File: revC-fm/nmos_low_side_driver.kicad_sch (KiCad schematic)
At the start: 6 parts, among them Q48 MMBT2907AM3T5G, Q49 MMDT3946

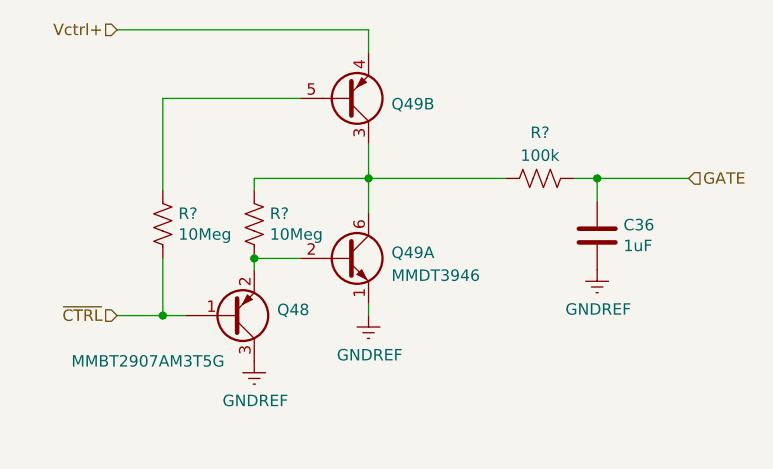
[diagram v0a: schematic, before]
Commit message: updated analog , solar comp, layout
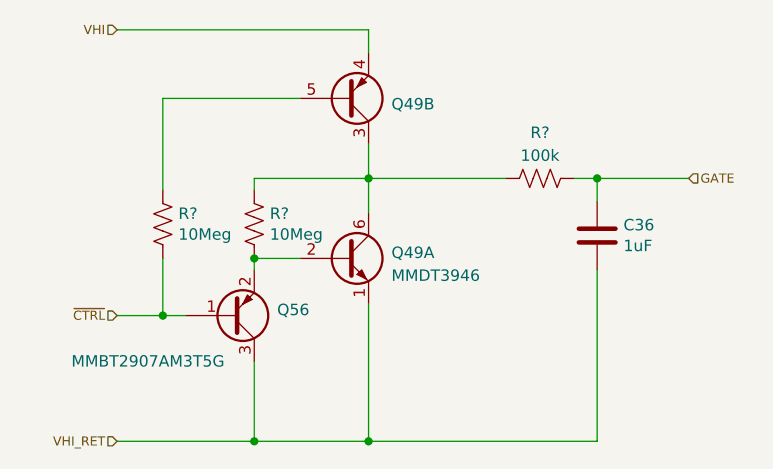
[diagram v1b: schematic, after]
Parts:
- renumbered Q48 to Q56
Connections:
- net GNDREF renamed VHI_RET
- net Vctrl+ renamed VHI

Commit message: routing
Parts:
- renumbered Q56 to Q58
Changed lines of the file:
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@@
         )
         (path "/d1441985-7b63-4bf8-a06d-c70da2e3b78b/00000000-0000-0000-0000-00005cec5dde/108189db-ac43-429a-bea6-7a20153b7e07/9a2f7458-daa0-4897-b1a7-e66c6dd2d928"
-          (reference "R219") (unit 1)
+          (reference "R213") (unit 1)
         )
       )
@@
         )
         (path "/d1441985-7b63-4bf8-a06d-c70da2e3b78b/00000000-0000-0000-0000-00005cec5dde/108189db-ac43-429a-bea6-7a20153b7e07/9a2f7458-daa0-4897-b1a7-e66c6dd2d928"
-          (reference "R220") (unit 1)
+          (reference "R214") (unit 1)
         )
       )
@@
   (symbol (lib_id "Device:Q_PNP_BEC") (at 120.65 105.41 0) (mirror x) (unit 1)
     (in_bom yes) (on_board yes) (dnp no)
-    (property "Reference" "Q56" (at 125.73 104.775 0)
+    (property "Reference" "Q58" (at 125.73 104.775 0)
       (effects (font (size 1.27 1.27)) (justify left))
     )
@@
       (project "mainboard"
         (path "/d1441985-7b63-4bf8-a06d-c70da2e3b78b/00000000-0000-0000-0000-00005cec5dde/108189db-ac43-429a-bea6-7a20153b7e07/9a2f7458-daa0-4897-b1a7-e66c6dd2d928"
-          (reference "Q56") (unit 1)
+          (reference "Q58") (unit 1)
         )
       )
@@
         )
         (path "/d1441985-7b63-4bf8-a06d-c70da2e3b78b/00000000-0000-0000-0000-00005cec5dde/108189db-ac43-429a-bea6-7a20153b7e07/9a2f7458-daa0-4897-b1a7-e66c6dd2d928"
-          (reference "R221") (unit 1)
+          (reference "R212") (unit 1)
         )
       )
@@
           (reference "C36") (unit 1)
         )
-        (path "/d1441985-7b63-4bf8-a06d-c70da2e3b78b/00000000-0000-0000-0000-00005cec5dde/b26c7749-01c8-494d-9e2e-e06c56569424"
-          (reference "C87") (unit 1)
-        )
         (path "/d1441985-7b63-4bf8-a06d-c70da2e3b78b/00000000-0000-0000-0000-00005cec5dde/108189db-ac43-429a-bea6-7a20153b7e07"
           (reference "C?") (unit 1)
@@
         )
         (path "/d1441985-7b63-4bf8-a06d-c70da2e3b78b/00000000-0000-0000-0000-00005cec5dde/108189db-ac43-429a-bea6-7a20153b7e07/9a2f7458-daa0-4897-b1a7-e66c6dd2d928"
-          (reference "C110") (unit 1)
-        )
-      )
+          (reference "C124") (unit 1)
+        )
+      )

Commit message: changed RF connector to TH
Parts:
- Q57: renamed from Q58; footprint Package_TO_SOT_SMD:SOT-723 -> SierraLobo:SOT-723
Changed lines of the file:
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@@
+      (effects (font (size 1.27 1.27)) hide)
+    )
+    (property "Mfr. Part No" "" (at 113.03 95.25 0)
       (effects (font (size 1.27 1.27)) hide)
     )
@@
         )
         (path "/d1441985-7b63-4bf8-a06d-c70da2e3b78b/00000000-0000-0000-0000-00005cec5dde/108189db-ac43-429a-bea6-7a20153b7e07/9a2f7458-daa0-4897-b1a7-e66c6dd2d928"
-          (reference "R213") (unit 1)
+          (reference "R209") (unit 1)
         )
       )
@@
     )
     (property "Datasheet" "http://www.diodes.com/_files/datasheets/ds30123.pdf" (at 133.35 99.06 0)
+      (effects (font (size 1.27 1.27)) hide)
+    )
+    (property "Mfr. Part No" "" (at 133.35 99.06 0)
       (effects (font (size 1.27 1.27)) hide)
     )
@@
         )
         (path "/d1441985-7b63-4bf8-a06d-c70da2e3b78b/00000000-0000-0000-0000-00005cec5dde/108189db-ac43-429a-bea6-7a20153b7e07/9a2f7458-daa0-4897-b1a7-e66c6dd2d928"
+          (reference "Q56") (unit 1)
+        )
+      )
+    )
+  )
+  (symbol (lib_id "Device:R_US") (at 123.19 95.25 0) (unit 1)
+    (in_bom yes) (on_board yes) (dnp no)
+    (property "Reference" "R?" (at 124.9172 94.0816 0)
+      (effects (font (size 1.27 1.27)) (justify left))
+    )
+    (property "Value" "10Meg" (at 124.9172 96.393 0)
+      (effects (font (size 1.27 1.27)) (justify left))
+    )
+    (property "Footprint" "Resistor_SMD:R_0603_1608Metric" (at 124.206 95.504 90)
+      (effects (font (size 1.27 1.27)) hide)
+    )
+    (property "Datasheet" "~" (at 123.19 95.25 0)
+      (effects (font (size 1.27 1.27)) hide)
+    )
+    (property "Mfr. Part No" "" (at 123.19 95.25 0)
+      (effects (font (size 1.27 1.27)) hide)
+    )
+    (pin "1")
+    (pin "2")
+    (instances
+      (project "mainboard"
+        (path "/d1441985-7b63-4bf8-a06d-c70da2e3b78b/00000000-0000-0000-0000-00005cec5dde/108189db-ac43-429a-bea6-7a20153b7e07"
+          (reference "R?") (unit 1)
+        )
+        (path "/d1441985-7b63-4bf8-a06d-c70da2e3b78b/00000000-0000-0000-0000-00005cec5dde/108189db-ac43-429a-bea6-7a20153b7e07/ea6bccc4-7d11-4c72-aac6-c14ca6d386f6"
+          (reference "R215") (unit 1)
+        )
+        (path "/d1441985-7b63-4bf8-a06d-c70da2e3b78b/00000000-0000-0000-0000-00005cec5dde/108189db-ac43-429a-bea6-7a20153b7e07/b16406a3-1a56-4ff9-817d-a6e31635f1dc"
+          (reference "R171") (unit 1)
+        )
+        (path "/d1441985-7b63-4bf8-a06d-c70da2e3b78b/00000000-0000-0000-0000-00005cec5dde/108189db-ac43-429a-bea6-7a20153b7e07/98075574-42bb-442c-ab5b-88185f36e4d7"
+          (reference "R177") (unit 1)
+        )
+        (path "/d1441985-7b63-4bf8-a06d-c70da2e3b78b/00000000-0000-0000-0000-00005cec5dde/108189db-ac43-429a-bea6-7a20153b7e07/58a3edb7-dfb1-4add-9075-2361d73480a6"
+          (reference "R204") (unit 1)
+        )
+        (path "/d1441985-7b63-4bf8-a06d-c70da2e3b78b/00000000-0000-0000-0000-00005cec5dde/108189db-ac43-429a-bea6-7a20153b7e07/68cb1cfa-66f3-4079-aaa8-5081a46702c5"
+          (reference "R183") (unit 1)
+        )
+        (path "/d1441985-7b63-4bf8-a06d-c70da2e3b78b/00000000-0000-0000-0000-00005cec5dde/108189db-ac43-429a-bea6-7a20153b7e07/9a2f7458-daa0-4897-b1a7-e66c6dd2d928"
+          (reference "R210") (unit 1)
+        )
+      )
+    )
+  )
+  (symbol (lib_id "Device:Q_PNP_BEC") (at 120.65 105.41 0) (mirror x) (unit 1)
+    (in_bom yes) (on_board yes) (dnp no)
+    (property "Reference" "Q57" (at 125.73 104.775 0)
+      (effects (font (size 1.27 1.27)) (justify left))
+    )
+    (property "Value" "MMBT2907AM3T5G" (at 102.87 110.49 0)
+      (effects (font (size 1.27 1.27)) (justify left))
+    )
+    (property "Footprint" "SierraLobo:SOT-723" (at 125.73 107.95 0)
+      (effects (font (size 1.27 1.27)) hide)
+    )
+    (property "Datasheet" "MMBT2907AM3T5G" (at 120.65 105.41 0)
+      (effects (font (size 1.27 1.27)) hide)
+    )
+    (property "Mfr. Part No" "" (at 120.65 105.41 0)
+      (effects (font (size 1.27 1.27)) hide)
+    )
+    (pin "1")
+    (pin "2")
+    (pin "3")
+    (instances
+      (project "mainboard"
+        (path "/d1441985-7b63-4bf8-a06d-c70da2e3b78b/00000000-0000-0000-0000-00005cec5dde/108189db-ac43-429a-bea6-7a20153b7e07/9a2f7458-daa0-4897-b1a7-e66c6dd2d928"
           (reference "Q57") (unit 1)
-        )
-      )
-    )
-  )
-  (symbol (lib_id "Device:R_US") (at 123.19 95.25 0) (unit 1)
-    (in_bom yes) (on_board yes) (dnp no)
-    (property "Reference" "R?" (at 124.9172 94.0816 0)
-      (effects (font (size 1.27 1.27)) (justify left))
-    )
-    (property "Value" "10Meg" (at 124.9172 96.393 0)
-      (effects (font (size 1.27 1.27)) (justify left))
-    )
-    (property "Footprint" "Resistor_SMD:R_0603_1608Metric" (at 124.206 95.504 90)
-      (effects (font (size 1.27 1.27)) hide)
-    )
-    (property "Datasheet" "~" (at 123.19 95.25 0)
-      (effects (font (size 1.27 1.27)) hide)
-    )
-    (pin "1")
-    (pin "2")
-    (instances
-      (project "mainboard"
-        (path "/d1441985-7b63-4bf8-a06d-c70da2e3b78b/00000000-0000-0000-0000-00005cec5dde/108189db-ac43-429a-bea6-7a20153b7e07"
-          (reference "R?") (unit 1)
-        )
-        (path "/d1441985-7b63-4bf8-a06d-c70da2e3b78b/00000000-0000-0000-0000-00005cec5dde/108189db-ac43-429a-bea6-7a20153b7e07/ea6bccc4-7d11-4c72-aac6-c14ca6d386f6"
-          (reference "R215") (unit 1)
-        )
-        (path "/d1441985-7b63-4bf8-a06d-c70da2e3b78b/00000000-0000-0000-0000-00005cec5dde/108189db-ac43-429a-bea6-7a20153b7e07/b16406a3-1a56-4ff9-817d-a6e31635f1dc"
-          (reference "R171") (unit 1)
-        )
-        (path "/d1441985-7b63-4bf8-a06d-c70da2e3b78b/00000000-0000-0000-0000-00005cec5dde/108189db-ac43-429a-bea6-7a20153b7e07/98075574-42bb-442c-ab5b-88185f36e4d7"
-          (reference "R177") (unit 1)
-        )
-        (path "/d1441985-7b63-4bf8-a06d-c70da2e3b78b/00000000-0000-0000-0000-00005cec5dde/108189db-ac43-429a-bea6-7a20153b7e07/58a3edb7-dfb1-4add-9075-2361d73480a6"
-          (reference "R204") (unit 1)
-        )
-        (path "/d1441985-7b63-4bf8-a06d-c70da2e3b78b/00000000-0000-0000-0000-00005cec5dde/108189db-ac43-429a-bea6-7a20153b7e07/68cb1cfa-66f3-4079-aaa8-5081a46702c5"
-          (reference "R183") (unit 1)
-        )
-        (path "/d1441985-7b63-4bf8-a06d-c70da2e3b78b/00000000-0000-0000-0000-00005cec5dde/108189db-ac43-429a-bea6-7a20153b7e07/9a2f7458-daa0-4897-b1a7-e66c6dd2d928"
-          (reference "R214") (unit 1)
-        )
-      )
-    )
-  )
-  (symbol (lib_id "Device:Q_PNP_BEC") (at 120.65 105.41 0) (mirror x) (unit 1)
-    (in_bom yes) (on_board yes) (dnp no)
-    (property "Reference" "Q58" (at 125.73 104.775 0)
-      (effects (font (size 1.27 1.27)) (justify left))
-    )
-    (property "Value" "MMBT2907AM3T5G" (at 102.87 110.49 0)
-      (effects (font (size 1.27 1.27)) (justify left))
-    )
-    (property "Footprint" "Package_TO_SOT_SMD:SOT-723" (at 125.73 107.95 0)
-      (effects (font (size 1.27 1.27)) hide)
-    )
-    (property "Datasheet" "MMBT2907AM3T5G" (at 120.65 105.41 0)
-      (effects (font (size 1.27 1.27)) hide)
-    )
-    (pin "1")
-    (pin "2")
-    (pin "3")
-    (instances
-      (project "mainboard"
-        (path "/d1441985-7b63-4bf8-a06d-c70da2e3b78b/00000000-0000-0000-0000-00005cec5dde/108189db-ac43-429a-bea6-7a20153b7e07/9a2f7458-daa0-4897-b1a7-e66c6dd2d928"
-          (reference "Q58") (unit 1)
         )
       )
@@
       (effects (font (size 1.27 1.27)) hide)
     )
+    (property "Mfr. Part No" "" (at 154.94 90.17 0)
+      (effects (font (size 1.27 1.27)) hide)
+    )
     (pin "1")
     (pin "2")
@@
         )
         (path "/d1441985-7b63-4bf8-a06d-c70da2e3b78b/00000000-0000-0000-0000-00005cec5dde/108189db-ac43-429a-bea6-7a20153b7e07/9a2f7458-daa0-4897-b1a7-e66c6dd2d928"
-          (reference "R212") (unit 1)
+          (reference "R208") (unit 1)
         )
       )
@@
     )
     (property "Datasheet" "http://www.diodes.com/_files/datasheets/ds30123.pdf" (at 133.35 81.28 0)
+      (effects (font (size 1.27 1.27)) hide)
+    )
+    (property "Mfr. Part No" "" (at 133.35 81.28 0)
       (effects (font (size 1.27 1.27)) hide)
     )
@@
         )
         (path "/d1441985-7b63-4bf8-a06d-c70da2e3b78b/00000000-0000-0000-0000-00005cec5dde/108189db-ac43-429a-bea6-7a20153b7e07/9a2f7458-daa0-4897-b1a7-e66c6dd2d928"
-          (reference "Q57") (unit 2)
+          (reference "Q56") (unit 2)
         )
       )
@@
     )
     (property "Datasheet" "" (at 161.29 96.52 0)
+      (effects (font (size 1.27 1.27)) hide)
+    )
+    (property "Mfr. Part No" "" (at 161.29 96.52 0)
       (effects (font (size 1.27 1.27)) hide)
     )
@@
         )
         (path "/d1441985-7b63-4bf8-a06d-c70da2e3b78b/00000000-0000-0000-0000-00005cec5dde/108189db-ac43-429a-bea6-7a20153b7e07/9a2f7458-daa0-4897-b1a7-e66c6dd2d928"
-          (reference "C124") (unit 1)
-        )
-      )
+          (reference "C114") (unit 1)
+        )
+      )

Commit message: working revC review changes
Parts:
- removed Q49: MMDT3946, Package_TO_SOT_SMD:SOT-363_SC-70-6, symbol Transistor_BJT:MMDT3946
- removed Q57: MMBT2907AM3T5G, SierraLobo:SOT-723, symbol Device:Q_PNP_BEC
- removed R?: 10Meg, Resistor_SMD:R_0603_1608Metric, symbol Device:R_US
- removed R?: 100k, Resistor_SMD:R_0603_1608Metric, symbol Device:R_US
- added Q39: MMDT3946, Package_TO_SOT_SMD:SOT-363_SC-70-6, symbol Transistor_BJT:MMDT3946
- added Q61, Q62: SSM3J15FV,L3F, Package_TO_SOT_SMD:SOT-723, symbol Device:Q_PMOS_GSD
- added R224, R225, R226: 100k, Resistor_SMD:R_0603_1608Metric, symbol Device:R_US
- added R?: 10Meg, Resistor_SMD:R_0603_1608Metric, symbol Device:R_US
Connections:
- net GATE: now also R226.2
- net VHI: now also R?.1, Q39.6 (C1), Q61.2 (S), Q62.2 (S)
- net VHI_RET: now also Q39.3 (C2), R?.2
- net ~{CTRL}: now also R224.1, R225.1
- new net: Q62.1 (G), R225.2
- new net: Q39.1 (E1), Q39.4 (E2), R226.1
- new net: Q39.2 (B1), Q39.5 (B2), Q61.3 (D), Q62.3 (D), R?.1
- new net: Q61.1 (G), R224.2
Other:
- note added: "Redundant PMOS"
- moved on the sheet: C36, R?

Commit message: working revC
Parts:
- removed Q61, Q62: SSM3J15FV,L3F, Package_TO_SOT_SMD:SOT-723, symbol Device:Q_PMOS_GSD
- added Q43: NX3008PBKS, Package_TO_SOT_SMD:SOT-363_SC-70-6, symbol SierraLobo:NX3008PBKS
- added R281: 0, Resistor_SMD:R_0603_1608Metric, symbol Device:R_US
- Q39: Mfr. Part No (none) -> MMDT3946-7-F
- R156: renamed from R224; footprint Resistor_SMD:R_0603_1608Metric -> Resistor_SMD:R_0402_1005Metric
- R157: renamed from R225; footprint Resistor_SMD:R_0603_1608Metric -> Resistor_SMD:R_0402_1005Metric
- R158: renamed from R226; footprint Resistor_SMD:R_0603_1608Metric -> Resistor_SMD:R_0402_1005Metric
- R? (x2): footprint Resistor_SMD:R_0603_1608Metric -> Resistor_SMD:R_0402_1005Metric
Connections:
- net VHI: now also R281.1; no longer Q39.6 (C1), R?.1
- net at R157.2: now also Q43.2 (G1)
- net at Q39.2 (B1), Q39.5 (B2), R?.1: now also Q43.3 (D2), Q43.6 (D1)
- net at R156.2: now also Q43.5 (G2)
- new net: Q39.6 (C1), Q43.1 (S1), Q43.4 (S2), R281.2, R?.1

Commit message: working
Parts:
- removed Q43: NX3008PBKS, Package_TO_SOT_SMD:SOT-363_SC-70-6, symbol SierraLobo:NX3008PBKS
- removed R156, R157: 100k, Resistor_SMD:R_0402_1005Metric, symbol Device:R_US
- removed R?: 10Meg, Resistor_SMD:R_0402_1005Metric, symbol Device:R_US
- added Q2 (x2): MMDT2907AQ, Package_TO_SOT_SMD:SOT-363_SC-70-6, symbol SierraLobo:MMDT2907
- added Q21, Q22: BSZ025N04LSATMA1, SierraLobo:PG-TSDSON-8_3.3x3.3mm, symbol SierraLobo:BSZ025
- added R87, R88: 1k, Resistor_SMD:R_0402_1005Metric, symbol Device:R_US
- added R? (x2): 1Meg, Resistor_SMD:R_0402_1005Metric, symbol Device:R_US
- R?: value 10Meg -> 1Meg
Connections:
- net at Q39.6 (C1), R281.2: now also Q2.1 (E1), Q2.1 (E1)
- net at Q39.2 (B1), Q39.5 (B2), R?.1: now also Q2.6 (C1), Q2.6 (C1)
- net GATE: no longer names the net of C36.1, R158.2
- net GATE: now also R87.1, R88.1
- net VHI_RET: no longer names the net of C36.2, Q39.3 (C2), R?.2
- new net: Q2.2 (B1), R?.2 (x2)
- new net: Q21.4 (G), R87.2
- new net: Q22.4 (G), R88.2
- new net RET: Q21.1 (S), Q22.1 (S)
- new net RET_INHIB: Q21.5 (D), Q22.5 (D)
- new net SW1: R?.1
- new net SW4: R?.1
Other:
- note removed: "Redundant PMOS"
- moved on the sheet: R281, R?
